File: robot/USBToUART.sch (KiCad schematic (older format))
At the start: 11 parts

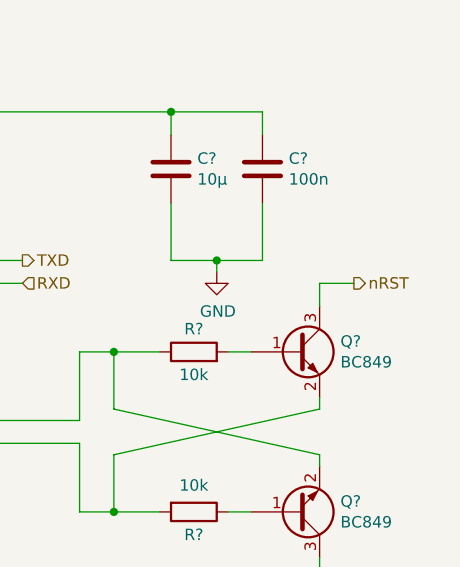
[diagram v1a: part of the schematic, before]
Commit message: UI parts, (re)wiring remaining signals
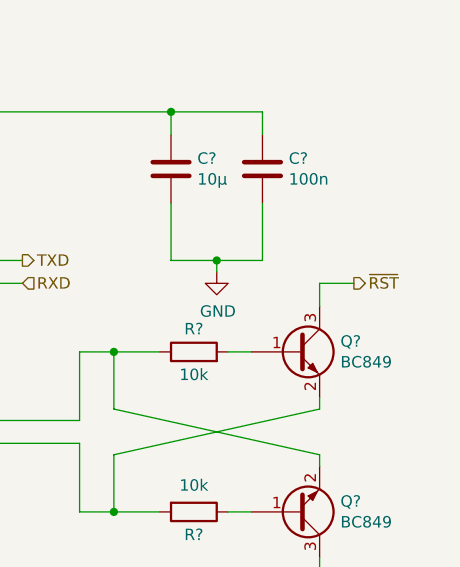
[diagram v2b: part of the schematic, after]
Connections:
- net nRST renamed ~RST
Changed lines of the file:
@@
 $Descr A4 11693 8268
 encoding utf-8
-Sheet 4 7
+Sheet 3 8
 Title "USB To UART"
 Date "2019-06-29"
@@
 	5000 4450 5100 4450
 Text HLabel 5550 3450 2    50   Output ~ 0
-nRST
+~RST
 Text HLabel 5550 4800 2    50   Output ~ 0
 GPIO0

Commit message: DRC check fixes and small changes
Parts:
- gave numbers to parts that had none: 11
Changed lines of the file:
@@
 $EndDescr
 $Comp
-L Interface_USB:CH340G U?
+L Interface_USB:CH340G U3
 U 1 1 5D17B663
 P 3450 3750
-F 0 "U?" H 3650 4450 50  0000 C CNN
+F 0 "U3" H 3650 4450 50  0000 C CNN
 F 1 "CH340G" H 3650 4350 50  0000 C CNN
 F 2 "Package_SO:SOIC-16_3.9x9.9mm_P1.27mm" H 3500 3200 50  0001 L CNN
@@
 $EndComp
 $Comp
-L Device:C C?
+L Device:C C3
 U 1 1 5D189DEC
 P 2600 2950
-F 0 "C?" H 2715 2996 50  0000 L CNN
+F 0 "C3" H 2715 2996 50  0000 L CNN
 F 1 "100n" H 2715 2905 50  0000 L CNN
 F 2 "" H 2638 2800 50  0001 C CNN
@@
 NoConn ~ 3050 3450
 $Comp
-L Device:C C?
+L Device:C C5
 U 1 1 5D18C358
 P 5150 2950
-F 0 "C?" H 5265 2996 50  0000 L CNN
+F 0 "C5" H 5265 2996 50  0000 L CNN
 F 1 "100n" H 5265 2905 50  0000 L CNN
 F 2 "" H 5188 2800 50  0001 C CNN
@@
 $EndComp
 $Comp
-L Device:C C?
+L Device:C C4
 U 1 1 5D18C6CF
 P 4750 2950
-F 0 "C?" H 4865 2996 50  0000 L CNN
+F 0 "C4" H 4865 2996 50  0000 L CNN
 F 1 "10µ" H 4865 2905 50  0000 L CNN
 F 2 "" H 4788 2800 50  0001 C CNN
@@
 	3850 3450 4100 3450
 $Comp
-L Transistor_BJT:BC849 Q?
+L Transistor_BJT:BC849 Q1
 U 1 1 5D1A1025
 P 5300 3750
-F 0 "Q?" H 5491 3796 50  0000 L CNN
+F 0 "Q1" H 5491 3796 50  0000 L CNN
 F 1 "BC849" H 5491 3705 50  0000 L CNN
 F 2 "Package_TO_SOT_SMD:SOT-23" H 5500 3675 50  0001 L CIN
@@
 $EndComp
 $Comp
-L Transistor_BJT:BC849 Q?
+L Transistor_BJT:BC849 Q2
 U 1 1 5D1A25D2
 P 5300 4450
-F 0 "Q?" H 5491 4404 50  0000 L CNN
+F 0 "Q2" H 5491 4404 50  0000 L CNN
 F 1 "BC849" H 5491 4495 50  0000 L CNN
 F 2 "Package_TO_SOT_SMD:SOT-23" H 5500 4375 50  0001 L CIN
@@
 $EndComp
 $Comp
-L Device:R R?
+L Device:R R5
 U 1 1 5D1A33B4
 P 4850 3750
-F 0 "R?" V 4950 3750 50  0000 C CNN
+F 0 "R5" V 4950 3750 50  0000 C CNN
 F 1 "10k" V 4750 3750 50  0000 C CNN
 F 2 "" V 4780 3750 50  0001 C CNN
@@
 $EndComp
 $Comp
-L Device:R R?
+L Device:R R6
 U 1 1 5D1A3B1C
 P 4850 4450
-F 0 "R?" V 4950 4450 50  0000 C CNN
+F 0 "R6" V 4950 4450 50  0000 C CNN
 F 1 "10k" V 4734 4450 50  0000 C CNN
 F 2 "" V 4780 4450 50  0001 C CNN
@@
 	3850 4150 4350 4150
 $Comp
-L Device:Crystal_GND24 Y?
+L Device:Crystal_GND24 Y1
 U 1 1 5D1B564B
 P 2100 4200
-F 0 "Y?" V 1950 4300 50  0000 L CNN
+F 0 "Y1" V 1950 4300 50  0000 L CNN
 F 1 "Crystal_GND24" V 1950 3550 50  0000 L CNN
 F 2 "" H 2100 4200 50  0001 C CNN
@@
 	1750 4200 1750 4300
 $Comp
-L Device:C C?
+L Device:C C7
 U 1 1 5D1BA8EA
 P 2750 4700
-F 0 "C?" H 2865 4746 50  0000 L CNN
+F 0 "C7" H 2865 4746 50  0000 L CNN
 F 1 "22p" H 2865 4655 50  0000 L CNN
 F 2 "" H 2788 4550 50  0001 C CNN
@@
 $EndComp
 $Comp
-L Device:C C?
+L Device:C C6
 U 1 1 5D1BB082
 P 1400 4700
-F 0 "C?" H 1515 4746 50  0000 L CNN
+F 0 "C6" H 1515 4746 50  0000 L CNN
 F 1 "22p" H 1515 4655 50  0000 L CNN
 F 2 "" H 1438 4550 50  0001 C CNN

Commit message: Testpoints, switch, small changes
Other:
- moved on the sheet: C3, C4, C5, C6, C7, Q1, Q2, R5, R6, U3, Y1
